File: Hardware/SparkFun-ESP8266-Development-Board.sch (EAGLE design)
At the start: 72 parts, among them J1 U.FL, Q1 2.5A/30V, U1 ESP8266, U2 MCP73831, U3 AT25SF041-SOIC8, U4 AP2112K-3.3V, U5 ATECC108-MAHDA, U6 TMP1021:1, U7 TSL2561FN, Y1 26MHz

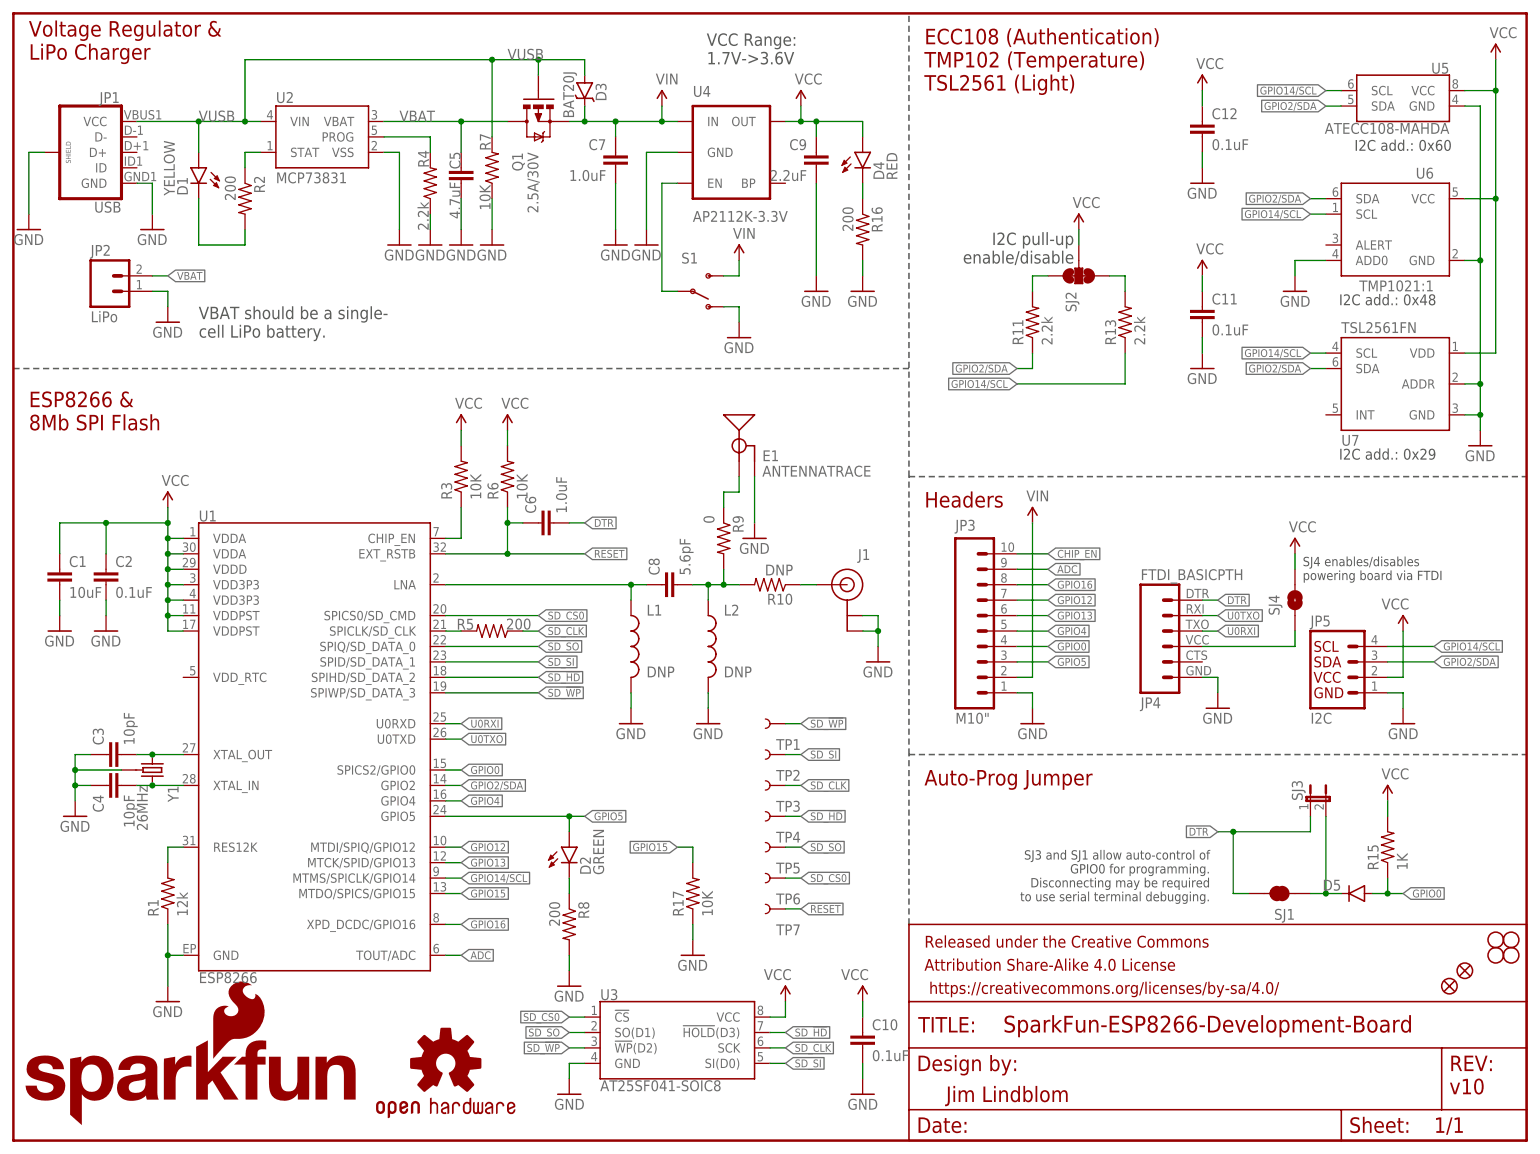
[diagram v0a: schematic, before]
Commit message: Removing silk labels on sensors. Changing R4 to 2k (charge at 500mA).
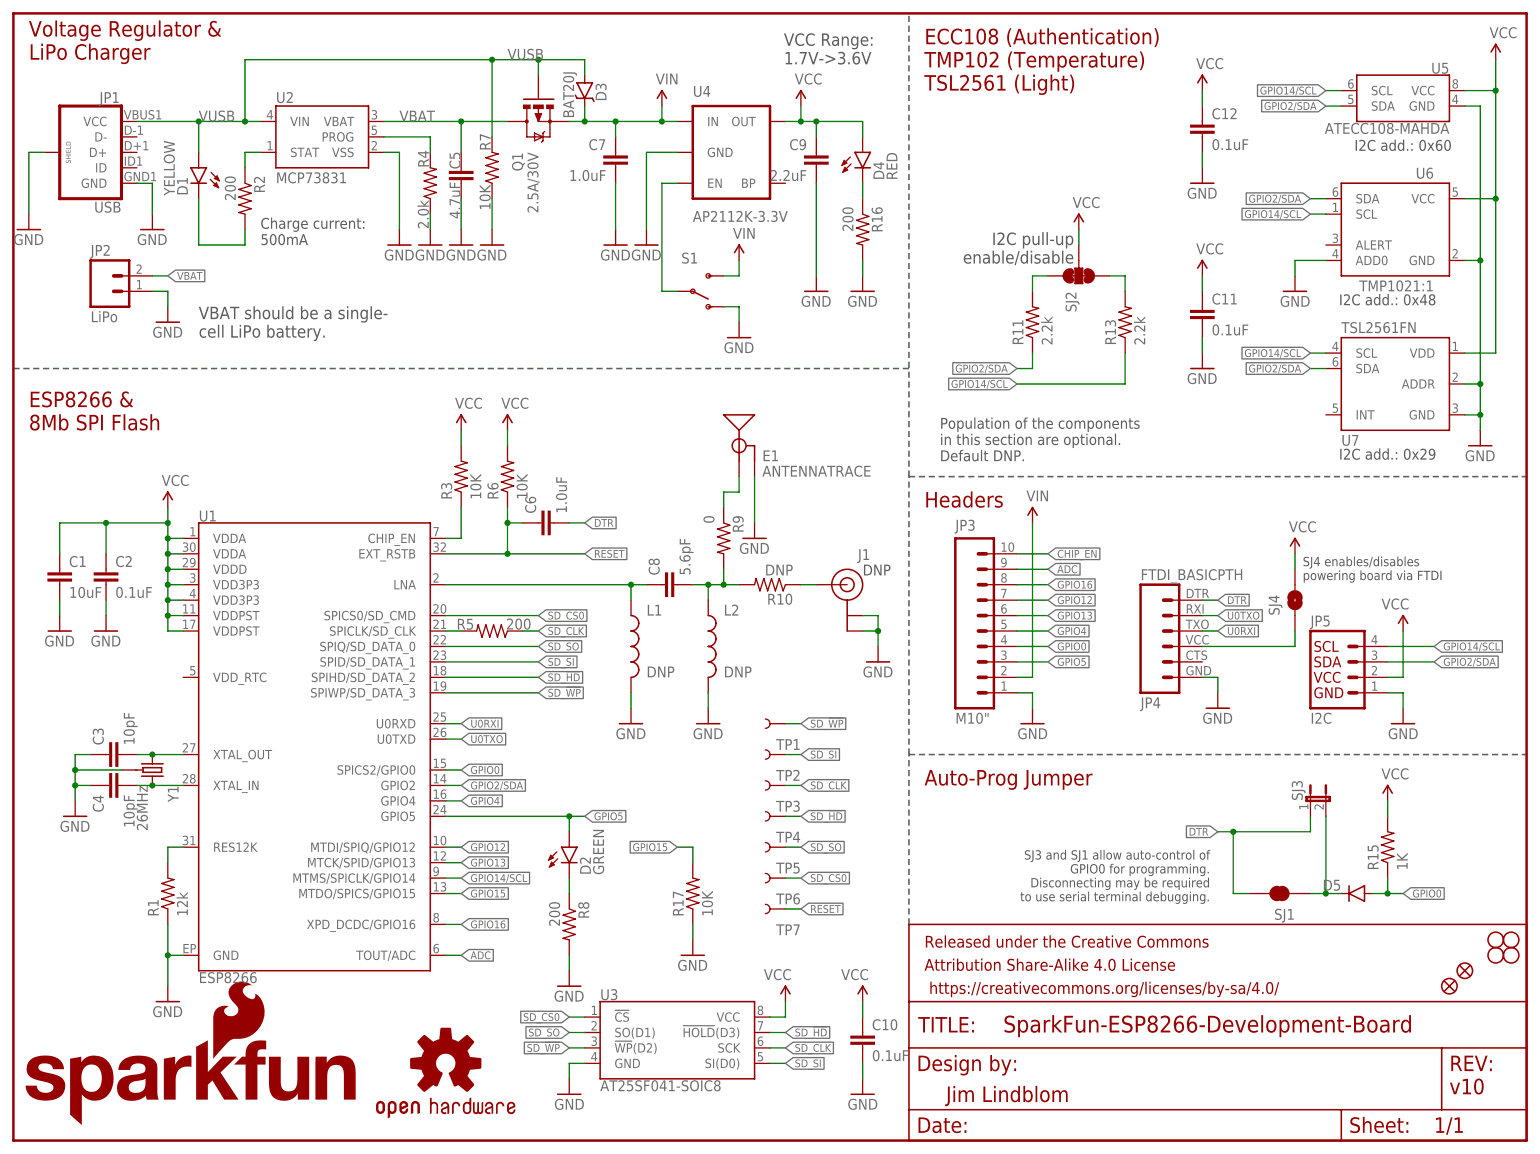
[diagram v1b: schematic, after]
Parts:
- J1: value U.FL -> DNP
- R4: value 2.2k -> 2.0k; device SparkFun-Resistors:2.2KOHM1/10W1%(0603) -> SparkFun-Resistors:2.0KOHM1/10W5%(0603)
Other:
- note added: "Charge current: 500mA"
- note added: "DNP"
- note added: "Population of the components in this section are optional. Default DNP."
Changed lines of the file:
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@@
 <layer number="223" name="223bmp" color="24" fill="1" visible="no" active="no"/>
 <layer number="224" name="224bmp" color="25" fill="1" visible="no" active="no"/>
+<layer number="225" name="225bmp" color="7" fill="1" visible="yes" active="yes"/>
+<layer number="226" name="226bmp" color="7" fill="1" visible="yes" active="yes"/>
+<layer number="227" name="227bmp" color="7" fill="1" visible="yes" active="yes"/>
+<layer number="228" name="228bmp" color="7" fill="1" visible="yes" active="yes"/>
+<layer number="229" name="229bmp" color="7" fill="1" visible="yes" active="yes"/>
+<layer number="230" name="230bmp" color="7" fill="1" visible="yes" active="yes"/>
+<layer number="231" name="231bmp" color="7" fill="1" visible="yes" active="yes"/>
 <layer number="248" name="Housing" color="7" fill="1" visible="yes" active="yes"/>
 <layer number="249" name="Edge" color="7" fill="1" visible="yes" active="yes"/>
@@
 <part name="GND13" library="SparkFun-Aesthetics" deviceset="GND" device=""/>
 <part name="GND17" library="SparkFun-Aesthetics" deviceset="GND" device=""/>
-<part name="J1" library="SparkFun-Connectors" deviceset="U.FL" device="" value="U.FL"/>
+<part name="J1" library="SparkFun-Connectors" deviceset="U.FL" device="" value="DNP"/>
 <part name="GND21" library="SparkFun-Aesthetics" deviceset="GND" device=""/>
 <part name="C6" library="SparkFun-Capacitors" deviceset="1.0UF-16V-10%(0603)" device="" value="1.0uF"/>
@@
 <part name="GND1" library="SparkFun-Aesthetics" deviceset="GND" device=""/>
 <part name="GND8" library="SparkFun-Aesthetics" deviceset="GND" device=""/>
-<part name="R4" library="SparkFun-Resistors" deviceset="2.2KOHM1/10W1%(0603)" device="" value="2.2k"/>
 <part name="GND9" library="SparkFun-Aesthetics" deviceset="GND" device=""/>
 <part name="GND10" library="SparkFun-Aesthetics" deviceset="GND" device=""/>
@@
 <part name="D2" library="SparkFun-LED" deviceset="LED-GREEN" device="0603" value="GREEN"/>
 <part name="SJ1" library="SparkFun-Passives" deviceset="JUMPER-PAD-2-NC_BY_TRACE" device="" value=""/>
+<part name="R4" library="SparkFun-Resistors" deviceset="2.0KOHM1/10W5%(0603)" device="" value="2.0k"/>
 </parts>
 <sheets>
@@
 <text x="149.86" y="58.42" size="2.54" layer="94">Auto-Prog Jumper</text>
 <text x="236.22" y="7.62" size="2.54" layer="94">v10</text>
-<text x="114.046" y="177.038" size="2.032" layer="97">VCC Range:
+<text x="126.746" y="177.038" size="2.032" layer="97">VCC Range:
 1.7V-&gt;3.6V</text>
 <text x="30.48" y="137.16" size="2.032" layer="97" align="top-left">VBAT should be a single-
@@
 <text x="228.6" y="164.592" size="1.778" layer="97" align="top-center">I2C add.: 0x60</text>
 <text x="226.06" y="113.792" size="1.778" layer="97" align="top-center">I2C add.: 0x29</text>
+<text x="152.4" y="111.76" size="1.778" layer="97">Population of the components
+in this section are optional.
+Default DNP.</text>
+<text x="40.64" y="147.32" size="1.778" layer="97">Charge current:
+500mA</text>
+<text x="139.7" y="92.964" size="1.778" layer="97">DNP</text>
 </plain>
 <instances>
@@
 <instance part="GND13" gate="1" x="101.6" y="68.58"/>
 <instance part="GND17" gate="1" x="114.3" y="68.58"/>
-<instance part="J1" gate="G$1" x="137.16" y="91.44" rot="MR0"/>
+<instance part="J1" gate="G$1" x="137.16" y="91.44" smashed="yes" rot="MR0">
+<attribute name="NAME" x="140.97" y="95.504" size="1.778" layer="95" rot="MR0"/>
+</instance>
 <instance part="GND21" gate="1" x="142.24" y="78.74"/>
 <instance part="C6" gate="G$1" x="88.9" y="101.6" rot="R90"/>
@@
 <instance part="GND1" gate="1" x="2.54" y="149.86"/>
 <instance part="GND8" gate="1" x="63.5" y="147.32"/>
-<instance part="R4" gate="G$1" x="68.58" y="157.48" smashed="yes" rot="R90">
-<attribute name="NAME" x="68.3514" y="160.02" size="1.778" layer="95" rot="R90"/>
-<attribute name="VALUE" x="68.326" y="154.432" size="1.778" layer="96" rot="MR270"/>
-</instance>
 <instance part="GND9" gate="1" x="68.58" y="147.32"/>
 <instance part="GND10" gate="1" x="73.66" y="147.32"/>
@@
 <instance part="D2" gate="G$1" x="91.44" y="48.26"/>
 <instance part="SJ1" gate="G$1" x="208.28" y="40.64" rot="R180"/>
+<instance part="R4" gate="G$1" x="68.58" y="157.48" smashed="yes" rot="R90">
+<attribute name="NAME" x="68.3514" y="160.02" size="1.778" layer="95" rot="R90"/>
+<attribute name="VALUE" x="68.326" y="154.686" size="1.778" layer="96" rot="MR270"/>
+</instance>
 </instances>
 <busses>
@@
 </segment>
 <segment>
-<pinref part="R4" gate="G$1" pin="1"/>
 <pinref part="GND9" gate="1" pin="GND"/>
 <wire x1="68.58" y1="149.86" x2="68.58" y2="152.4" width="0.1524" layer="91"/>
+<pinref part="R4" gate="G$1" pin="1"/>
 </segment>
 <segment>
@@
 <pinref part="U2" gate="G$1" pin="PROG"/>
 <wire x1="60.96" y1="165.1" x2="68.58" y2="165.1" width="0.1524" layer="91"/>
+<wire x1="68.58" y1="162.56" x2="68.58" y2="165.1" width="0.1524" layer="91"/>
 <pinref part="R4" gate="G$1" pin="2"/>
-<wire x1="68.58" y1="162.56" x2="68.58" y2="165.1" width="0.1524" layer="91"/>
-</segment>
-</net>
+</segment>
+</net>

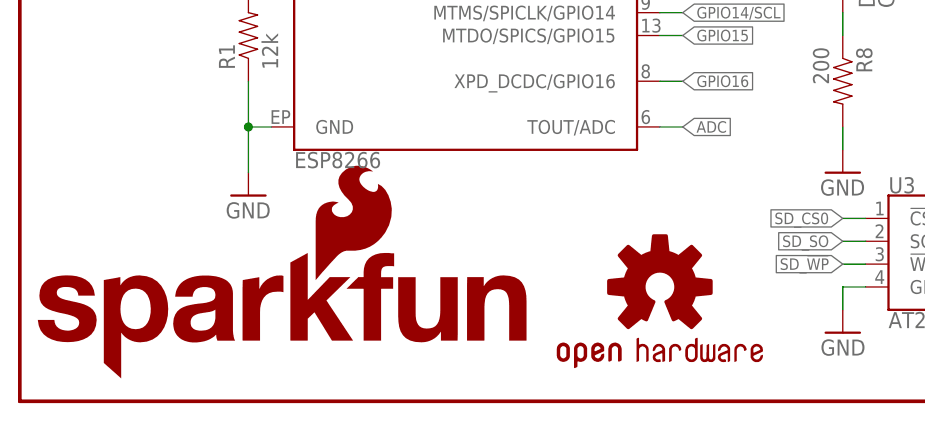
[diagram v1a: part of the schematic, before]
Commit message: Adding PROD_ID to U1, S1, and Y1.
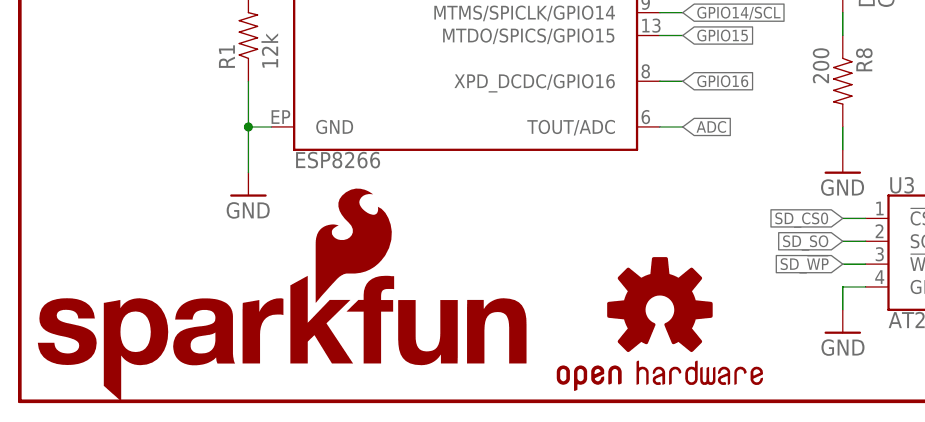
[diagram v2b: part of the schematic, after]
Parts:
- S1: PROD_ID (none) -> SWCH-10651
- U4: PROD_ID (none) -> VREG-12457
- Y1: PROD_ID (none) -> XTAL-12454
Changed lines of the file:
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@@
 <part name="GND7" library="SparkFun-Aesthetics" deviceset="GND" device=""/>
 <part name="GND3" library="SparkFun-Aesthetics" deviceset="GND" device=""/>
-<part name="Y1" library="things" deviceset="CRYSTAL-GROUNDED" device="3.2X2.5" value="26MHz"/>
+<part name="Y1" library="things" deviceset="CRYSTAL-GROUNDED" device="3.2X2.5" value="26MHz">
+<attribute name="PROD_ID" value="XTAL-12454"/>
+</part>
 <part name="GND2" library="SparkFun-Aesthetics" deviceset="GND" device=""/>
 <part name="GND4" library="SparkFun-Aesthetics" deviceset="GND" device=""/>
@@
 <part name="TP3" library="SparkFun-Passives" deviceset="TEST-POINT" device="3X5" value=""/>
 <part name="TP4" library="SparkFun-Passives" deviceset="TEST-POINT" device="3X5" value=""/>
-<part name="U4" library="SparkFun-PowerIC" deviceset="V_REG_LDO" device="SMD" value="AP2112K-3.3V"/>
+<part name="U4" library="SparkFun-PowerIC" deviceset="V_REG_LDO" device="SMD" value="AP2112K-3.3V">
+<attribute name="PROD_ID" value="VREG-12457"/>
+</part>
 <part name="C10" library="SparkFun-Capacitors" deviceset="0.1UF-25V(+80/-20%)(0603)" device="" value="0.1uF"/>
 <part name="C11" library="SparkFun-Capacitors" deviceset="0.1UF-25V(+80/-20%)(0603)" device="" value="0.1uF"/>
@@
 <part name="D5" library="SparkFun-DiscreteSemi" deviceset="DIODE" device="BAS16"/>
 <part name="SJ4" library="SparkFun-Passives" deviceset="JUMPER-PAD-2-NO" device="YES_SILK" value=""/>
-<part name="S1" library="SparkFun-Electromechanical" deviceset="SWITCH-SPDT" device="-SMD-A"/>
+<part name="S1" library="SparkFun-Electromechanical" deviceset="SWITCH-SPDT" device="-SMD-A">
+<attribute name="PROD_ID" value="SWCH-10651"/>
+</part>
 <part name="SJ3" library="SparkFun-Passives" deviceset="JUMPER-PTH-2-NC" device="" value=""/>
 <part name="SUPPLY12" library="SparkFun-Aesthetics" deviceset="VIN" device=""/>
@@
 <instance part="GND7" gate="1" x="25.4" y="22.86"/>
 <instance part="GND3" gate="1" x="10.16" y="53.34"/>
-<instance part="Y1" gate="G$1" x="22.86" y="60.96" rot="R270"/>
+<instance part="Y1" gate="G$1" x="22.86" y="60.96" rot="R270">
+<attribute name="PROD_ID" x="22.86" y="60.96" size="1.778" layer="96" rot="R270" display="off"/>
+</instance>
 <instance part="GND2" gate="1" x="7.62" y="83.82"/>
 <instance part="GND4" gate="1" x="15.24" y="83.82"/>
@@
 <instance part="SUPPLY8" gate="G$1" x="167.64" y="101.6"/>
 <instance part="GND22" gate="1" x="167.64" y="68.58" rot="MR0"/>
-<instance part="LOGO1" gate="G$1" x="0" y="2.54"/>
-<instance part="LOGO3" gate="G$1" x="32.512" y="12.954"/>
-<instance part="LOGO4" gate="G$1" x="71.12" y="12.7"/>
+<instance part="LOGO1" gate="G$1" x="0" y="0"/>
+<instance part="LOGO3" gate="G$1" x="32.512" y="10.414"/>
+<instance part="LOGO4" gate="G$1" x="71.12" y="10.16"/>
 <instance part="E1" gate="G$1" x="119.38" y="119.38"/>
 <instance part="GND18" gate="1" x="121.92" y="99.06"/>
@@
 <instance part="TP3" gate="G$1" x="127" y="58.42" rot="R180"/>
 <instance part="TP4" gate="G$1" x="127" y="53.34" rot="R180"/>
-<instance part="U4" gate="G$1" x="119.38" y="162.56"/>
+<instance part="U4" gate="G$1" x="119.38" y="162.56">
+<attribute name="PROD_ID" x="119.38" y="162.56" size="1.778" layer="96" display="off"/>
+</instance>
 <instance part="C10" gate="G$1" x="139.7" y="15.24"/>
 <instance part="C11" gate="G$1" x="195.58" y="134.62"/>
@@
 <instance part="D5" gate="G$1" x="220.98" y="40.64" rot="MR0"/>
 <instance part="SJ4" gate="G$1" x="210.82" y="88.9" rot="R90"/>
-<instance part="S1" gate="1" x="111.76" y="139.7" rot="MR180"/>
+<instance part="S1" gate="1" x="111.76" y="139.7" rot="MR180">
+<attribute name="PROD_ID" x="111.76" y="139.7" size="1.778" layer="96" rot="MR180" display="off"/>
+</instance>
 <instance part="SJ3" gate="G$1" x="213.36" y="55.88"/>
 <instance part="SUPPLY12" gate="G$1" x="119.38" y="144.78"/>
